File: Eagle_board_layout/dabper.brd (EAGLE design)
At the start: 127.9 x 135.9 mm, 4 parts, among them IC1 ATMEGA328-AU, IC2 MAX31855, K1 AQ1AD2-3

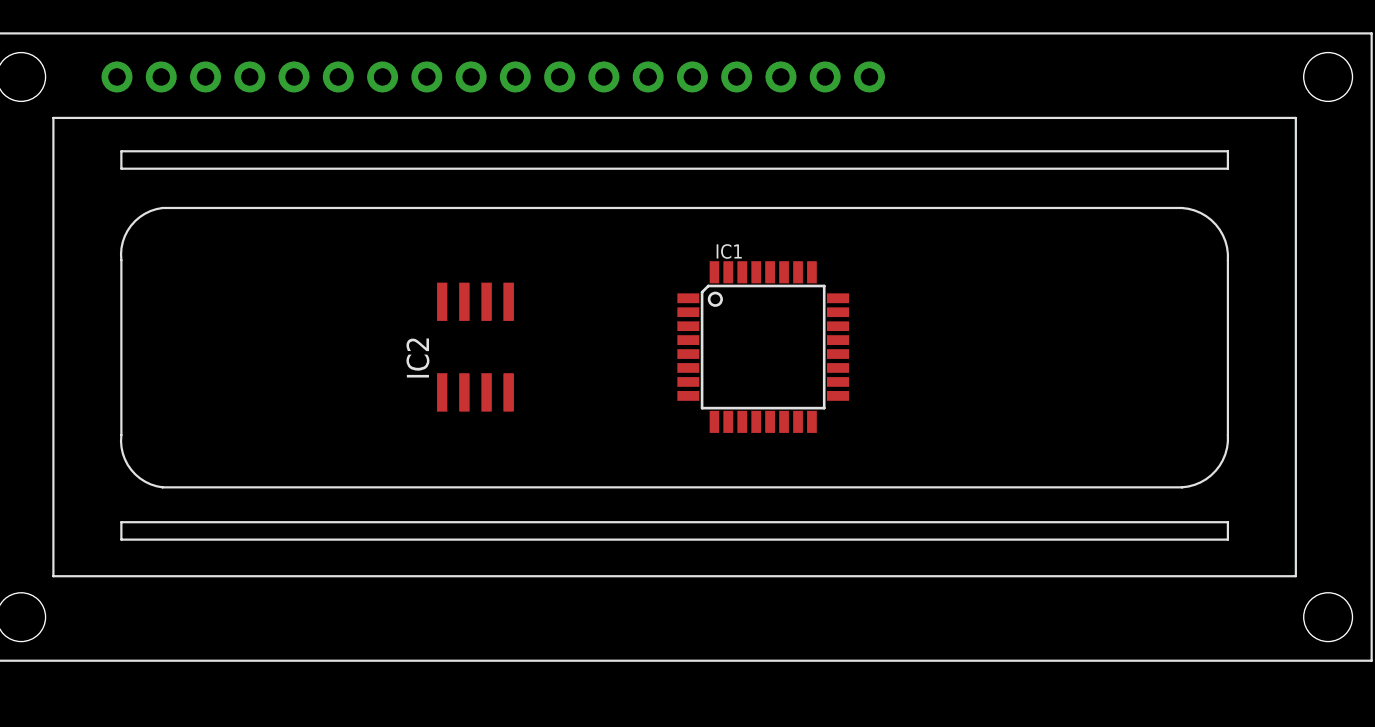
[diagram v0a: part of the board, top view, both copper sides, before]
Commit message: adding buttons and finalizing parts needed on PCB
Signed-off-by: Bryan Smith <zarboz@gmail.com>
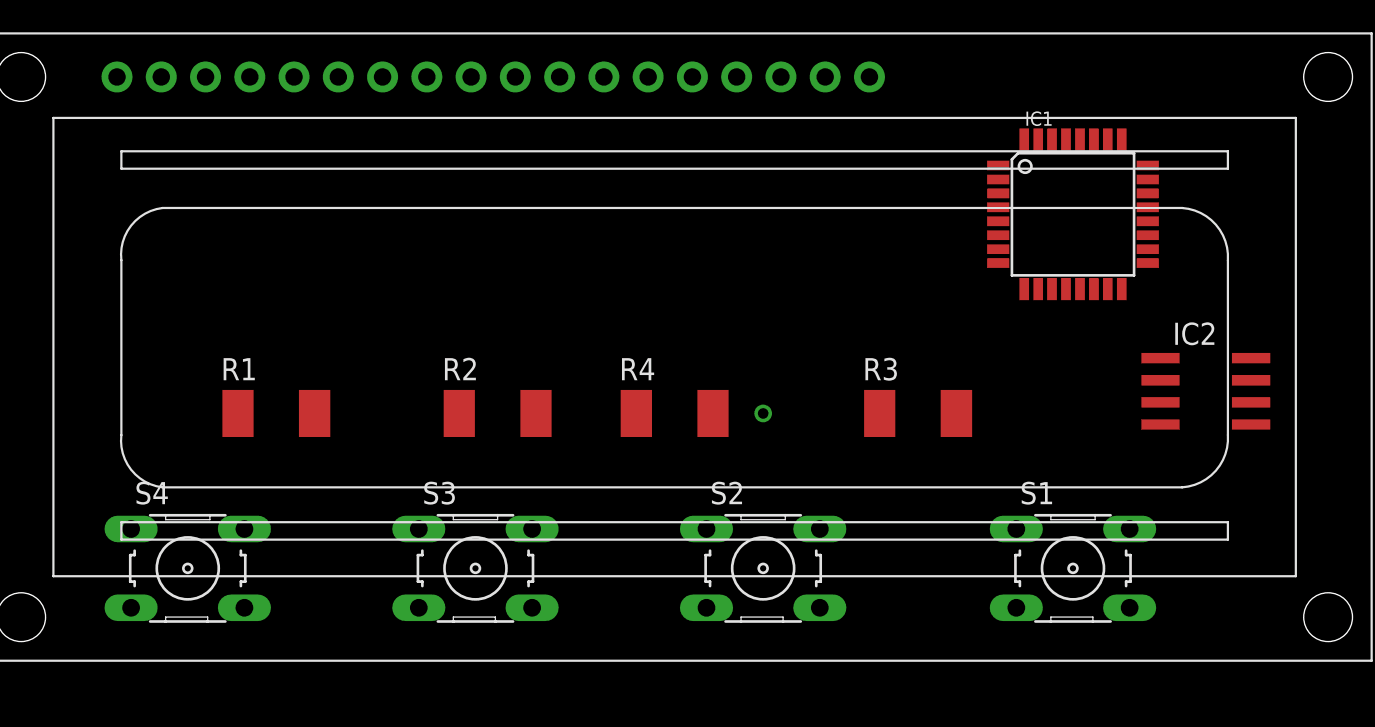
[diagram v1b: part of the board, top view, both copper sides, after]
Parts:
- added R1, R4: 1K Ohm, eagle-ltspice:R5025
- added R2: 470 Ohm, eagle-ltspice:R5025
- added R3: 330 Ohm, eagle-ltspice:R5025
- added S1: Switch 1, switch-omron:B3F-10XX
- added S2: Switch 2, switch-omron:B3F-10XX
- added S3: Switch 3, switch-omron:B3F-10XX
- added S4: Switch 4, switch-omron:B3F-10XX
- moved IC2 42.0 mm to (80.0, 25.4), turned to 270 degrees
- moved IC1 19.3 mm to (72.4, 35.6)
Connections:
- net N$2 renamed GND1
- removed net +5V: IC1.4, IC2.1, IC2.4, K1.3, U$1.1
- removed net -5V: IC1.5
- removed net N$16: IC2.5
- removed net N$17: IC1.26, K1.4
- removed net N$6 (its old number): IC1.13, U$1.16
- new net N$11: IC1.1, IC1.2, U$1.14, U$1.6
- new net N$12: IC1.9, U$1.13
- new net N$2: R2.2, R3.1, S3.1
- new net VSS: IC1.32, IC1.4, IC2.4, R4.2, U$1.1, U$1.15, U$1.4
- net N$1: now also IC1.27, R3.2, R4.1, S4.1; no longer IC1.32, U$1.4
- net N$10: now also IC1.13, IC1.14, U$1.16, U$1.17; no longer IC1.9, U$1.12
- net N$13: now also IC1.11, U$1.11; no longer IC1.24
- net N$14: now also K1.1; no longer IC1.25
- net N$15: now also IC1.26, K1.2; no longer IC2.6
- net N$3: now also R1.2, R2.1, S2.1; no longer IC1.1, IC1.2, U$1.11, U$1.6
- net N$4: now also R1.1, S1.1; no longer IC1.15, U$1.18
- net N$5: now also IC1.5, IC2.1, S1.2, S2.2, S3.2, S4.2, U$1.3, U$1.5; no longer IC1.10, IC1.14, U$1.13, U$1.17
- net N$7: now also IC1.25, IC2.5; no longer U$1.5
- net N$8: now also IC1.24, IC2.6; no longer U$1.15
- net N$9: now also IC1.10, IC1.15, U$1.12, U$1.18; no longer IC1.11, U$1.14
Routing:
- net N$2: track 0.00 -> 0.34 mm, vias 0 -> 1
